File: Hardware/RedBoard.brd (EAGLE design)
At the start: 68.6 x 53.3 mm, 78 parts, among them J1 AMP FCI 10103594-0001LF, J2 ISP, J3 POWER_JACKSUPER_BOMB_DIGITY, Q1 1A/60V/500mΩ, Q2 2N7002PW, Q3 2N7002PW, U1 CH340G, U2 LM1117, U3 AP2112-3.3V, U4 ATMEGA328P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

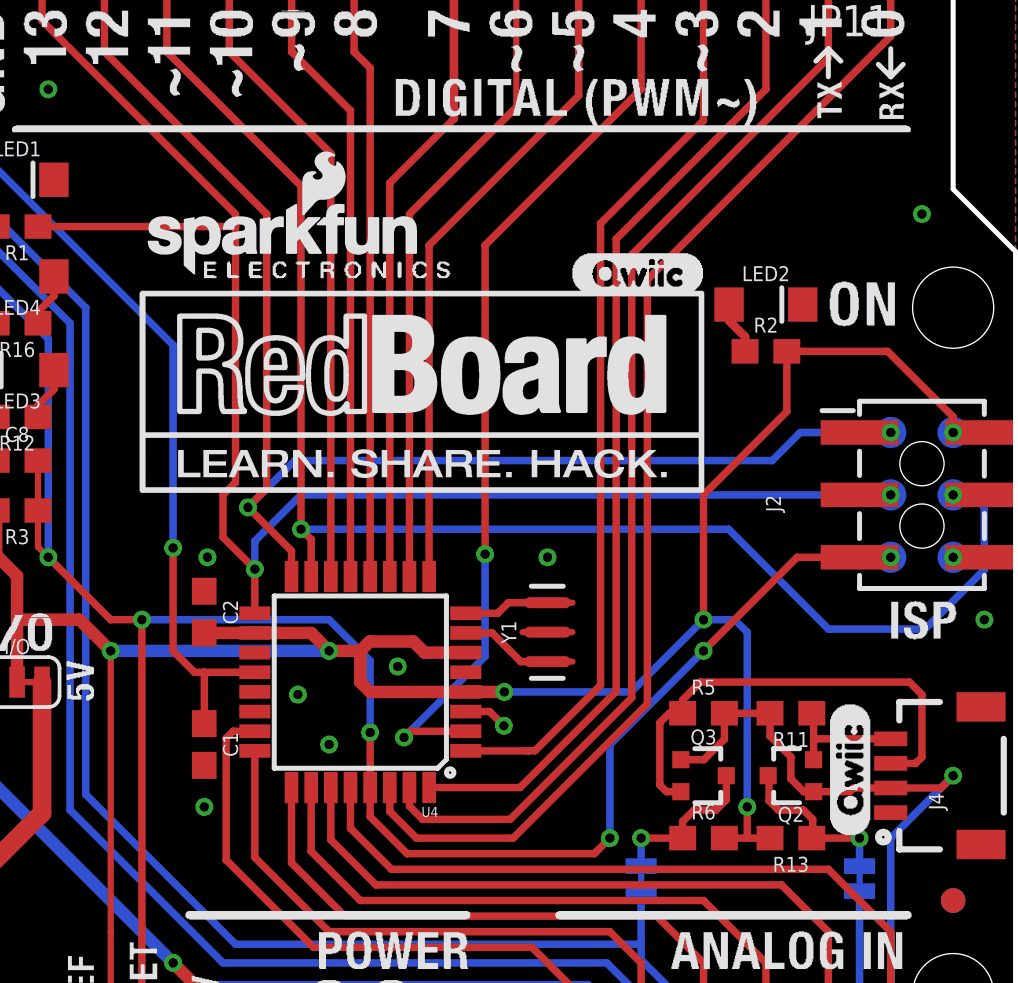
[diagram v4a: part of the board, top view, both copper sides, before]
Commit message: Updated SFE and QWIIC logos to vector to help with cam job times
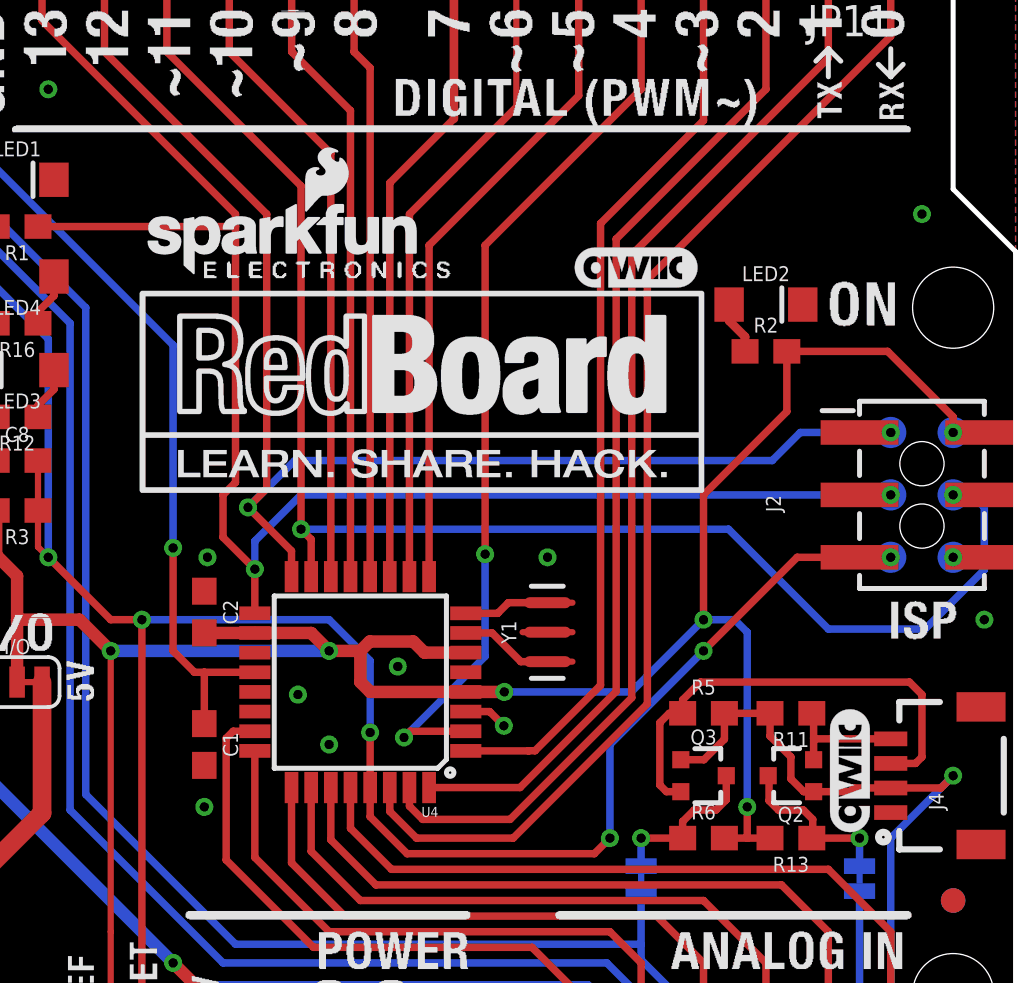
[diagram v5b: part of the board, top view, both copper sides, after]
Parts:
- removed JP1: SFE_LOGO_NAME.1_INCH, SparkFun-Aesthetics:SFE_LOGO_NAME_.1
- removed JP7: SFE_LOGO_FLAME.1_INCH, SparkFun-Aesthetics:SFE_LOGO_FLAME_.1
- removed U$1, U$2, U$3: (no value), Labels-0_04:(QWIIC)
- added LOGO2: SFE_LOGO_NAME_FLAME.1_INCH, SparkFun-Aesthetics:SFE_LOGO_NAME_FLAME_.1
- added LOGO3, LOGO4, LOGO5: QWIIC_LOGO_5MM, SparkFun-Aesthetics:QWIIC_5MM
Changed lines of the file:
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@@
 <layer number="27" name="tValues" color="7" fill="1" visible="no" active="yes"/>
 <layer number="28" name="bValues" color="7" fill="1" visible="no" active="yes"/>
-<layer number="29" name="tStop" color="2" fill="3" visible="yes" active="yes"/>
+<layer number="29" name="tStop" color="2" fill="3" visible="no" active="yes"/>
 <layer number="30" name="bStop" color="5" fill="6" visible="no" active="yes"/>
-<layer number="31" name="tCream" color="7" fill="4" visible="yes" active="yes"/>
+<layer number="31" name="tCream" color="7" fill="4" visible="no" active="yes"/>
 <layer number="32" name="bCream" color="7" fill="5" visible="no" active="yes"/>
 <layer number="33" name="tFinish" color="6" fill="3" visible="no" active="yes"/>
@@
 <layer number="44" name="Drills" color="7" fill="1" visible="no" active="yes"/>
 <layer number="45" name="Holes" color="7" fill="1" visible="yes" active="yes"/>
-<layer number="46" name="Milling" color="3" fill="1" visible="yes" active="yes"/>
+<layer number="46" name="Milling" color="3" fill="1" visible="no" active="yes"/>
 <layer number="47" name="Measures" color="7" fill="1" visible="no" active="yes"/>
 <layer number="48" name="Document" color="7" fill="1" visible="no" active="yes"/>
@@
 <attribute name="VALUE" x="50.8" y="22.352" size="0.6096" layer="27" font="vector" ratio="20" rot="R90" align="top-center"/>
 </element>
-<element name="JP1" library="SparkFun-Aesthetics" package="SFE_LOGO_NAME_.1" value="SFE_LOGO_NAME.1_INCH" x="32.7914" y="36.449" smashed="yes"/>
-<element name="JP7" library="SparkFun-Aesthetics" package="SFE_LOGO_FLAME_.1" value="SFE_LOGO_FLAME.1_INCH" x="39.2684" y="38.989" smashed="yes"/>
 <element name="J2" library="SparkFun-Connectors" package="2X3_SMT_POSTS" value="ISP" x="64.77" y="27.94" smashed="yes" rot="R270">
 <attribute name="NAME" x="58.42" y="27.94" size="0.6096" layer="25" rot="R270"/>
@@
 <attribute name="VALUE" x="55.88" y="13.208" size="0.6096" layer="27" font="vector" ratio="20" align="top-center"/>
 </element>
-<element name="U$2" library="Labels-0_04" package="(QWIIC)" value="" x="61.849" y="13.97" smashed="yes" rot="R90"/>
 <element name="FRAME2" library="SparkFun-Aesthetics" package="CREATIVE_COMMONS" value="FRAME-LETTER" x="1.016" y="-16.764" smashed="yes">
 <attribute name="DESIGNER" value="" x="1.016" y="-16.764" size="1.778" layer="27" display="off"/>
@@
 </element>
 <element name="LOGO1" library="SparkFun-Aesthetics" package="REVISION" value="REVISION" x="12.446" y="-19.939" smashed="yes"/>
-<element name="U$1" library="Labels-0_04" package="(QWIIC)" value="" x="50.419" y="36.957" smashed="yes"/>
-<element name="U$3" library="Labels-0_04" package="(QWIIC)" value="" x="38.989" y="46.482" smashed="yes" rot="MR0"/>
 <element name="U$4" library="buzzard_labels_J12" package="J120" value="" x="60.706" y="11.303" smashed="yes" rot="MR90"/>
 <element name="U$9" library="buzzard_labels_J14" package="J140" value="" x="51.816" y="11.176" smashed="yes" rot="MR90"/>
@@
 <attribute name="VALUE" x="17.78" y="41.0972" size="0.4318" layer="27" rot="R90" align="top-left"/>
 </element>
+<element name="LOGO2" library="SparkFun-Aesthetics" package="SFE_LOGO_NAME_FLAME_.1" value="SFE_LOGO_NAME_FLAME.1_INCH" x="38.8112" y="38.3794" smashed="yes"/>
+<element name="LOGO3" library="SparkFun-Aesthetics" package="QWIIC_5MM" value="QWIIC_LOGO_5MM" x="61.8236" y="16.6878" smashed="yes" rot="R90"/>
+<element name="LOGO4" library="SparkFun-Aesthetics" package="QWIIC_5MM" value="QWIIC_LOGO_5MM" x="53.1114" y="37.211" smashed="yes"/>
+<element name="LOGO5" library="SparkFun-Aesthetics" package="QWIIC_5MM" value="QWIIC_LOGO_5MM" x="36.2712" y="46.6598" smashed="yes" rot="MR0"/>
 </elements>
 <signals>
